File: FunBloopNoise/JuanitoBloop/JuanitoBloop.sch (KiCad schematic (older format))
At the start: 3 parts

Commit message: completed first pass at entering original schematic
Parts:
- added C1, C2, C6, C7, C8: 100nF, Capacitor_THT:C_Rect_L7.0mm_W2.5mm_P5.00mm, symbol Device:C
- added C3, C4: 10uF, Capacitor_THT:CP_Radial_D5.0mm_P2.50mm, symbol Device:CP
- added C5: 2.2nF, Capacitor_THT:C_Rect_L7.0mm_W2.5mm_P5.00mm, symbol Device:C
- added J1: Trig, Connector_PinHeader_2.54mm:PinHeader_1x02_P2.54mm_Vertical, symbol Connector:Conn_01x02_Male
- added J2: CV, Connector_PinHeader_2.54mm:PinHeader_1x02_P2.54mm_Vertical, symbol Connector:Conn_01x02_Male
- added J3: Out, Connector_PinHeader_2.54mm:PinHeader_1x02_P2.54mm_Vertical, symbol Connector:Conn_01x02_Male
- added Q1, Q2: 2N3904, Package_TO_SOT_THT:TO-92_Inline, symbol Transistor_BJT:2N3904
- added R10, R9: 10k, Resistor_THT:R_Axial_DIN0207_L6.3mm_D2.5mm_P10.16mm_Horizontal, symbol Device:R
- added R11: 1k, Resistor_THT:R_Axial_DIN0207_L6.3mm_D2.5mm_P10.16mm_Horizontal, symbol Device:R
- added R4, R8: 100k, Resistor_THT:R_Axial_DIN0207_L6.3mm_D2.5mm_P10.16mm_Horizontal, symbol Device:R
- added R5: 150R, Resistor_THT:R_Axial_DIN0207_L6.3mm_D2.5mm_P10.16mm_Horizontal, symbol Device:R
- added R6: 4.7k, Resistor_THT:R_Axial_DIN0207_L6.3mm_D2.5mm_P10.16mm_Horizontal, symbol Device:R
- added R7: 33k, Resistor_THT:R_Axial_DIN0207_L6.3mm_D2.5mm_P10.16mm_Horizontal, symbol Device:R
- added RV1, RV2, RV3: 100k, Connector_PinHeader_2.54mm:PinHeader_1x03_P2.54mm_Vertical, symbol Device:R_POT
- added U1: NE555, Package_DIP:DIP-8_W7.62mm_Socket_LongPads, symbol Timer:NE555
- added U2: 4046, Package_DIP:DIP-16_W7.62mm_Socket_LongPads, symbol 4xxx:4046
- added U3: NE5532, Package_DIP:DIP-8_W7.62mm_Socket_LongPads, symbol Amplifier_Operational:NE5532
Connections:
- net labels added: +12V, GND
- wire segments 0 -> 50
- no-connect marks 0 -> 9
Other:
- moved on the sheet: R1, R2, R3

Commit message: schematic v2 and pcb v1
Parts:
- added J4: Power, Connector_PinHeader_2.54mm:PinHeader_2x05_P2.54mm_Vertical, symbol Connector_Generic:Conn_02x05_Odd_Even
- U1: symbol Timer:NE555 -> JuanitoBloop-rescue:NE555-Timer
- U2: symbol 4xxx:4046 -> JuanitoBloop-rescue:4046-4xxx
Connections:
- net labels added: -12V
- wire segments 50 -> 54
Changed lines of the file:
@@
 EESchema Schematic File Version 4
-LIBS:JuanitoBloop-cache
-EELAYER 26 0
+EELAYER 30 0
 EELAYER END
 $Descr A4 11693 8268
@@
 $EndComp
 $Comp
-L Timer:NE555 U1
+L JuanitoBloop-rescue:NE555-Timer U1
 U 1 1 5FB01084
 P 4200 3300
@@
 $EndComp
 $Comp
-L 4xxx:4046 U2
+L JuanitoBloop-rescue:4046-4xxx U2
 U 1 1 5FB039AE
 P 7600 2400
@@
 Wire Wire Line
 	4700 3100 5600 3100
+$Comp
+L power:+12V #PWR0123
+U 1 1 5FB05556
+P 7750 4550
+F 0 "#PWR0123" H 7750 4400 50  0001 C CNN
+F 1 "+12V" H 7765 4723 50  0000 C CNN
+F 2 "" H 7750 4550 50  0001 C CNN
+F 3 "" H 7750 4550 50  0001 C CNN
+	1    7750 4550
+	1    0    0    -1
+$EndComp
+Connection ~ 7750 4550
+$Comp
+L power:-12V #PWR0124
+U 1 1 5FB062B4
+P 7750 5150
+F 0 "#PWR0124" H 7750 5250 50  0001 C CNN
+F 1 "-12V" H 7765 5323 50  0000 C CNN
+F 2 "" H 7750 5150 50  0001 C CNN
+F 3 "" H 7750 5150 50  0001 C CNN
+	1    7750 5150
+	-1   0    0    1
+$EndComp
+Connection ~ 7750 5150
+$Comp
+L Connector_Generic:Conn_02x05_Odd_Even J4
+U 1 1 5FB08BE6
+P 2150 1850
+F 0 "J4" H 2200 2267 50  0000 C CNN
+F 1 "Power" H 2200 2176 50  0000 C CNN
+F 2 "Connector_PinHeader_2.54mm:PinHeader_2x05_P2.54mm_Vertical" H 2150 1850 50  0001 C CNN
+F 3 "~" H 2150 1850 50  0001 C CNN
+	1    2150 1850
+	1    0    0    -1
+$EndComp
+$Comp
+L power:+12V #PWR0125
+U 1 1 5FB09E35
+P 2450 1650
+F 0 "#PWR0125" H 2450 1500 50  0001 C CNN
+F 1 "+12V" H 2465 1823 50  0000 C CNN
+F 2 "" H 2450 1650 50  0001 C CNN
+F 3 "" H 2450 1650 50  0001 C CNN
+	1    2450 1650
+	1    0    0    -1
+$EndComp
+$Comp
+L power:GND #PWR0126
+U 1 1 5FB0A6CF
+P 2450 1850
+F 0 "#PWR0126" H 2450 1600 50  0001 C CNN
+F 1 "GND" H 2455 1677 50  0000 C CNN
+F 2 "" H 2450 1850 50  0001 C CNN
+F 3 "" H 2450 1850 50  0001 C CNN
+	1    2450 1850
+	0    -1   -1   0
+$EndComp
+Wire Wire Line
+	2450 1750 2450 1850
+Connection ~ 2450 1850
+Wire Wire Line
+	2450 1850 2450 1950
+$Comp
+L power:+12V #PWR0127
+U 1 1 5FB0BE18
+P 1950 1650
+F 0 "#PWR0127" H 1950 1500 50  0001 C CNN
+F 1 "+12V" H 1965 1823 50  0000 C CNN
+F 2 "" H 1950 1650 50  0001 C CNN
+F 3 "" H 1950 1650 50  0001 C CNN
+	1    1950 1650
+	1    0    0    -1
+$EndComp
+$Comp
+L power:-12V #PWR0128
+U 1 1 5FB0C752
+P 2450 2050
+F 0 "#PWR0128" H 2450 2150 50  0001 C CNN
+F 1 "-12V" H 2465 2223 50  0000 C CNN
+F 2 "" H 2450 2050 50  0001 C CNN
+F 3 "" H 2450 2050 50  0001 C CNN
+	1    2450 2050
+	-1   0    0    1
+$EndComp
+$Comp
+L power:-12V #PWR0129
+U 1 1 5FB0CEBE
+P 1950 2050
+F 0 "#PWR0129" H 1950 2150 50  0001 C CNN
+F 1 "-12V" H 1965 2223 50  0000 C CNN
+F 2 "" H 1950 2050 50  0001 C CNN
+F 3 "" H 1950 2050 50  0001 C CNN
+	1    1950 2050
+	-1   0    0    1
+$EndComp
+$Comp
+L power:GND #PWR0130
+U 1 1 5FB0D314
+P 1950 1850
+F 0 "#PWR0130" H 1950 1600 50  0001 C CNN
+F 1 "GND" H 1955 1677 50  0000 C CNN
+F 2 "" H 1950 1850 50  0001 C CNN
+F 3 "" H 1950 1850 50  0001 C CNN
+	1    1950 1850
+	0    1    1    0
+$EndComp
+Wire Wire Line
+	1950 1750 1950 1850
+Connection ~ 1950 1850
+Wire Wire Line
+	1950 1850 1950 1950
 $EndSCHEMATC

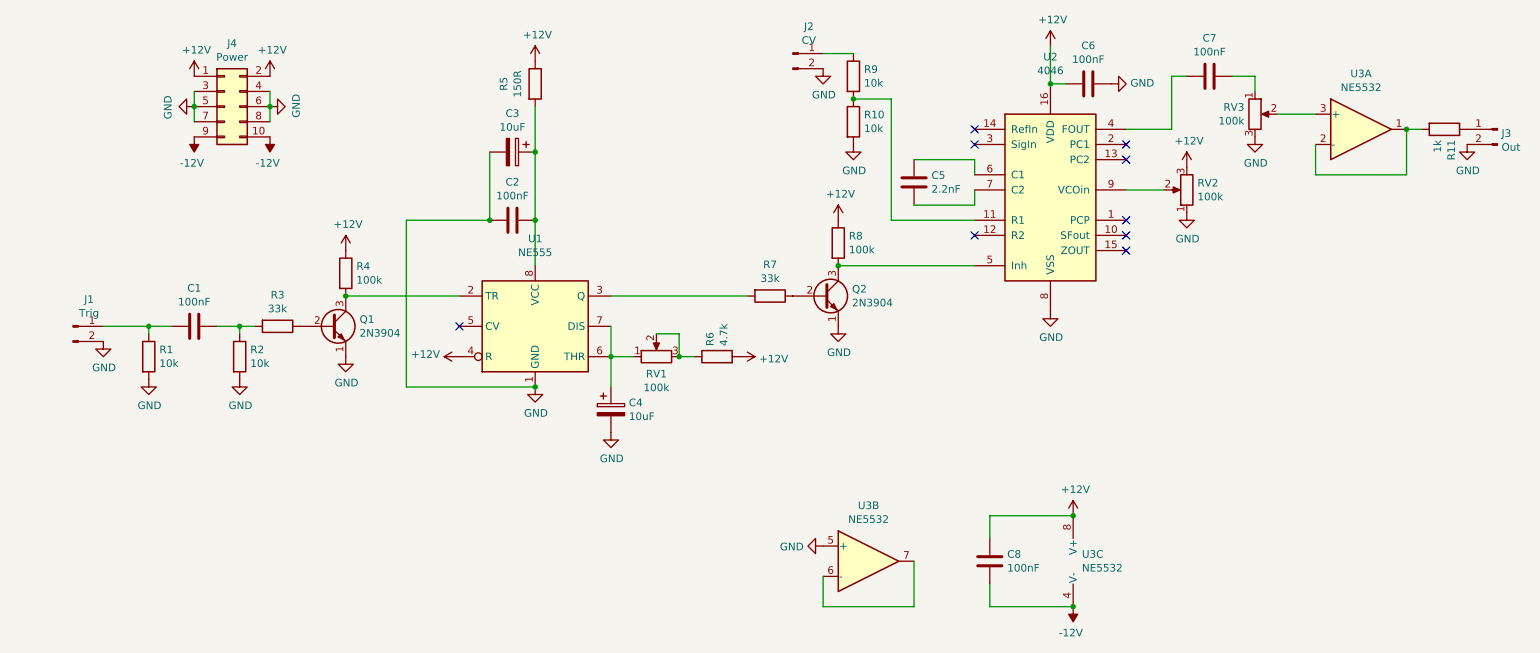
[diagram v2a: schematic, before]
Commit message: added ground plane, schematic documentation
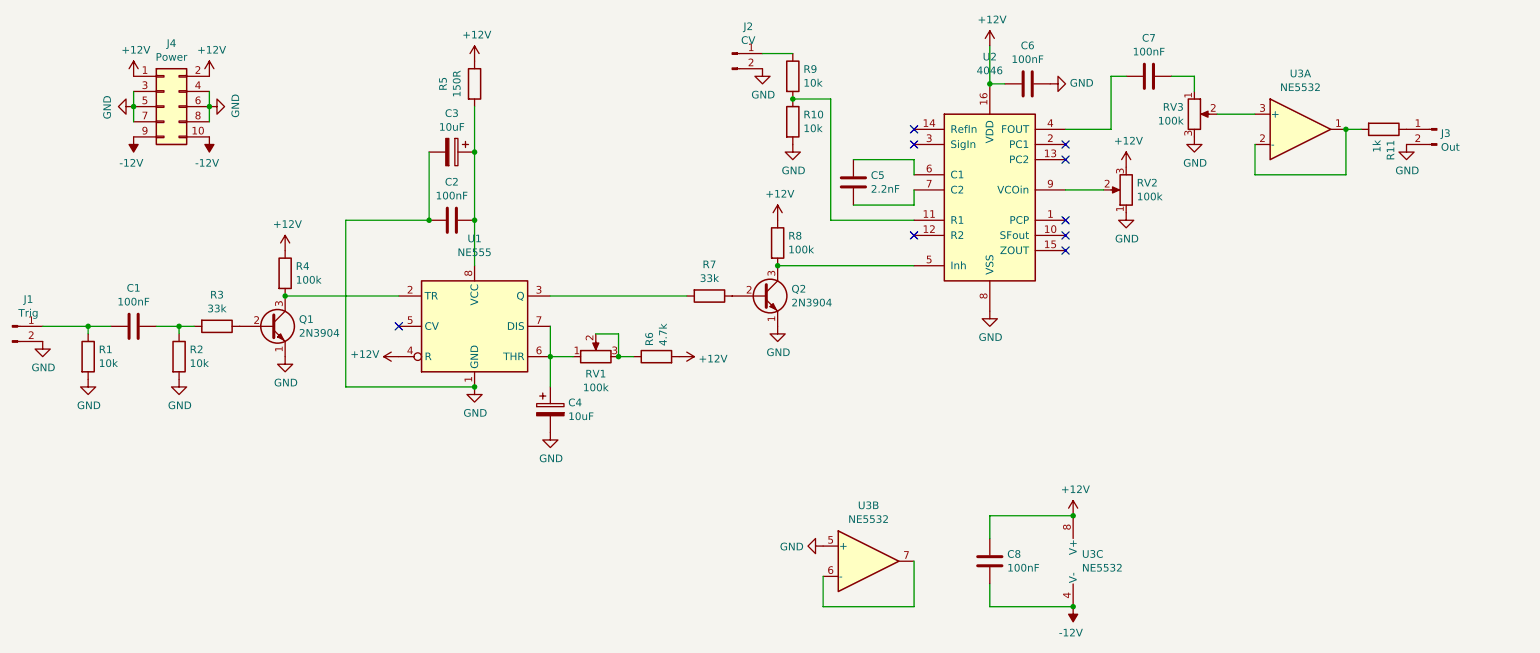
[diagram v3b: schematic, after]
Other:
- moved on the sheet: C1, C2, C3, C4, C5, C6, C7, J1, J2, J3, J4, Q1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
